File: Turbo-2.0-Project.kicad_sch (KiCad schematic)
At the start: 28 parts, among them Q1 BC337, Q2 BC337

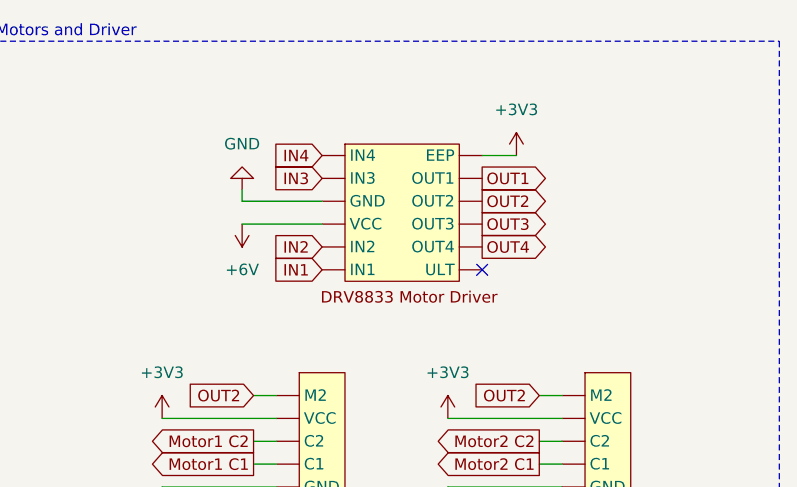
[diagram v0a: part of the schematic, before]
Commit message: Added Drv8833 footprints
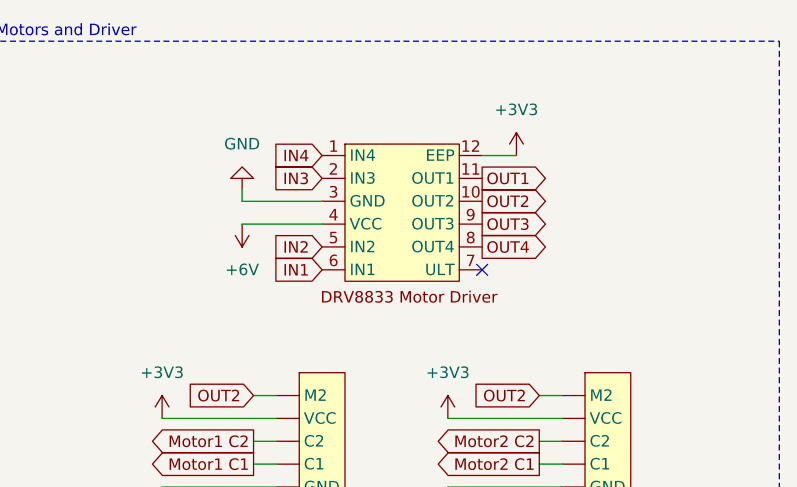
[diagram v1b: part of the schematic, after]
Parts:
- U1: footprint (none) -> turbo_custom_footprints:ESP32S3_Mini_Zero
- U2: footprint (none) -> turbo_custom_footprints:DRV8833_Motor_Driver
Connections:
- net +3V3: now also U2.12 (EEP); no longer U2. (ULT)
- net +6V: now also U2.4 (VCC); no longer U2. (ULT)
- net GND: now also U2.3 (GND); no longer U2. (ULT)
- net IN1: now also U2.6 (IN1); no longer U2. (ULT)
- net IN2: now also U2.5 (IN2); no longer U2. (ULT)
- net IN3: now also U2.2 (IN3); no longer U2. (ULT)
- net IN4: now also U2.1 (IN4); no longer U2. (ULT)
- net OUT1: now also U2.11 (OUT1); no longer U2. (ULT)
- net OUT2: now also U2.10 (OUT2); no longer U2. (ULT)
- net OUT3: now also U2.9 (OUT3); no longer U2. (ULT)
- net OUT4: now also U2.8 (OUT4); no longer U2. (ULT)
- new net: U6. (3), U7. (Vo+), U8. (Vo+)
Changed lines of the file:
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@@
 			)
 		)
-		(property "Footprint" ""
+		(property "Footprint" "turbo_custom_footprints:ESP32S3_Mini_Zero"
 			(at 44.45 53.34 0)
 			(effects
@@
 	)
 	(symbol
+		(lib_name "MotorPin6_1")
 		(lib_id "Turbo_Custom_Library:MotorPin6")
 		(at 231.14 68.58 0)
@@
 	)
 	(symbol
-		(lib_name "MotorPin6_1")
 		(lib_id "Turbo_Custom_Library:MotorPin6")
 		(at 262.89 68.58 0)
@@
 			)
 		)
-		(property "Footprint" ""
+		(property "Footprint" "turbo_custom_footprints:DRV8833_Motor_Driver"
 			(at 240.03 44.45 0)
 			(effects
@@
 			)
 		)
-		(pin ""
-		)
-		(pin ""
-		)
-		(pin ""
-		)
-		(pin ""
-		)
-		(pin ""
-		)
-		(pin ""
-		)
-		(pin ""
-		)
-		(pin ""
-		)
-		(pin ""
-		)
-		(pin ""
-		)
-		(pin ""
-		)
-		(pin ""
-		)
-		(instances
+		(pin "7"
+		)
+		(pin "6"
+		)
+		(pin "3"
+		)
+		(pin "2"
+		)
+		(pin "5"
+		)
+		(pin "10"
+		)
+		(pin "9"
+		)
+		(pin "1"
+		)
+		(pin "4"
+		)
+		(pin "12"
+		)
+		(pin "11"
+		)
+		(pin "8"
+		)
+		(instances
